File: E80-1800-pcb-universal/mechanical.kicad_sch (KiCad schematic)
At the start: 5 parts

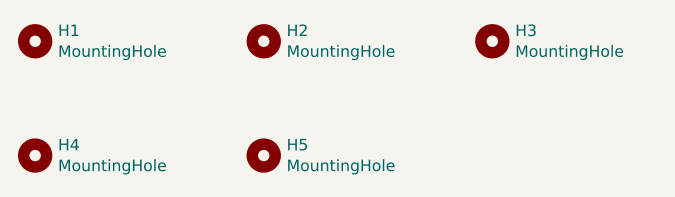
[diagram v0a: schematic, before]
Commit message: update to PCM marbastlib and KC8
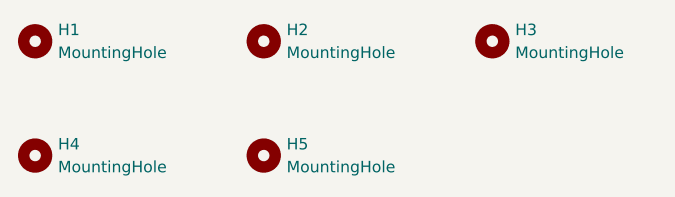
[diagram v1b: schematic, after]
